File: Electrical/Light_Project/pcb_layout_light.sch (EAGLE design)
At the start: 6 parts, among them U1 REG710NA-3.3/3K, U2 ATTINY85V-10SU

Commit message: Route PCB (not optimized)
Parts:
- added U3: FSM8JRT, button:FSM8JRT
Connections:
- net N$1: now also U3.2
- net N$4: now also U1.ENABLE
- net N$5: now also U3.1
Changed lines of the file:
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@@
 <part name="R1" library="10k Resistor" deviceset="CF14JT10K0" device=""/>
 <part name="C3" library="22ufcap" deviceset="C410C224M5U5TA7200" device=""/>
+<part name="U3" library="button" deviceset="FSM8JRT" device=""/>
 </parts>
 <sheets>
@@
 <attribute name="NAME" x="102.5906" y="88.4428" size="3.4798" layer="95" ratio="10" rot="SR0"/>
 </instance>
+<instance part="U3" gate="A" x="243.84" y="-2.54" smashed="yes" rot="R90">
+<attribute name="NAME" x="234.7214" y="15.5956" size="2.0828" layer="95" ratio="6" rot="SR90"/>
+<attribute name="VALUE" x="237.2614" y="14.9606" size="2.0828" layer="96" ratio="6" rot="SR90"/>
+</instance>
 </instances>
 <busses>
@@
 <pinref part="U2" gate="A" pin="VCC"/>
 <wire x1="7.62" y1="27.94" x2="218.44" y2="27.94" width="0.1524" layer="91"/>
-<wire x1="218.44" y1="27.94" x2="218.44" y2="10.16" width="0.1524" layer="91"/>
+<wire x1="218.44" y1="27.94" x2="218.44" y2="-5.08" width="0.1524" layer="91"/>
 <junction x="7.62" y="91.44"/>
 <junction x="218.44" y="-5.08"/>
-<junction x="218.44" y="10.16"/>
-<wire x1="218.44" y1="10.16" x2="218.44" y2="-5.08" width="0.1524" layer="91"/>
-<wire x1="218.44" y1="10.16" x2="228.6" y2="10.16" width="0.1524" layer="91"/>
-<wire x1="228.6" y1="10.16" x2="228.6" y2="-2.54" width="0.1524" layer="91"/>
-<junction x="228.6" y="-2.54"/>
+<wire x1="218.44" y1="27.94" x2="218.44" y2="43.18" width="0.1524" layer="91"/>
+<junction x="218.44" y="27.94"/>
+<wire x1="218.44" y1="43.18" x2="243.84" y2="43.18" width="0.1524" layer="91"/>
+<pinref part="U3" gate="A" pin="2"/>
+<wire x1="243.84" y1="43.18" x2="243.84" y2="40.64" width="0.1524" layer="91"/>
 </segment>
 </net>
@@
 <junction x="78.74" y="83.82"/>
 <junction x="86.36" y="96.52"/>
+<pinref part="U1" gate="A" pin="ENABLE"/>
+<wire x1="12.7" y1="81.28" x2="12.7" y2="71.12" width="0.1524" layer="91"/>
+<wire x1="12.7" y1="71.12" x2="86.36" y2="71.12" width="0.1524" layer="91"/>
+<wire x1="86.36" y1="71.12" x2="86.36" y2="83.82" width="0.1524" layer="91"/>
+<junction x="86.36" y="83.82"/>
 </segment>
 </net>
@@
 <junction x="218.44" y="-12.7"/>
 <junction x="228.6" y="-12.7"/>
+<pinref part="U3" gate="A" pin="1"/>
+<wire x1="228.6" y1="-12.7" x2="243.84" y2="-12.7" width="0.1524" layer="91"/>
+<wire x1="243.84" y1="-12.7" x2="243.84" y2="0" width="0.1524" layer="91"/>
 </segment>
 </net>

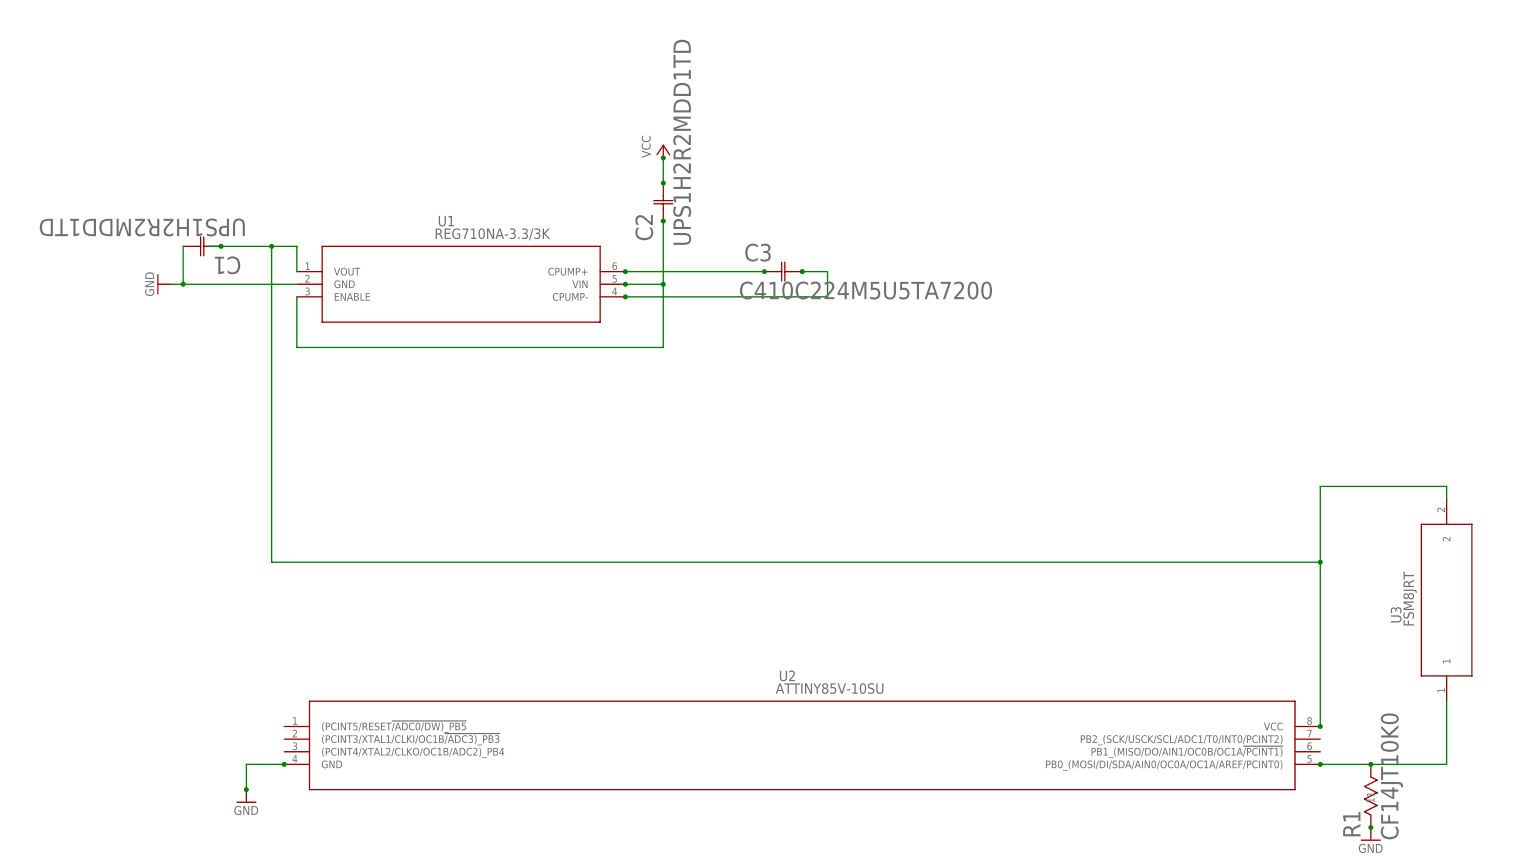
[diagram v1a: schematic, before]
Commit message: use surface mount resistor in diagram
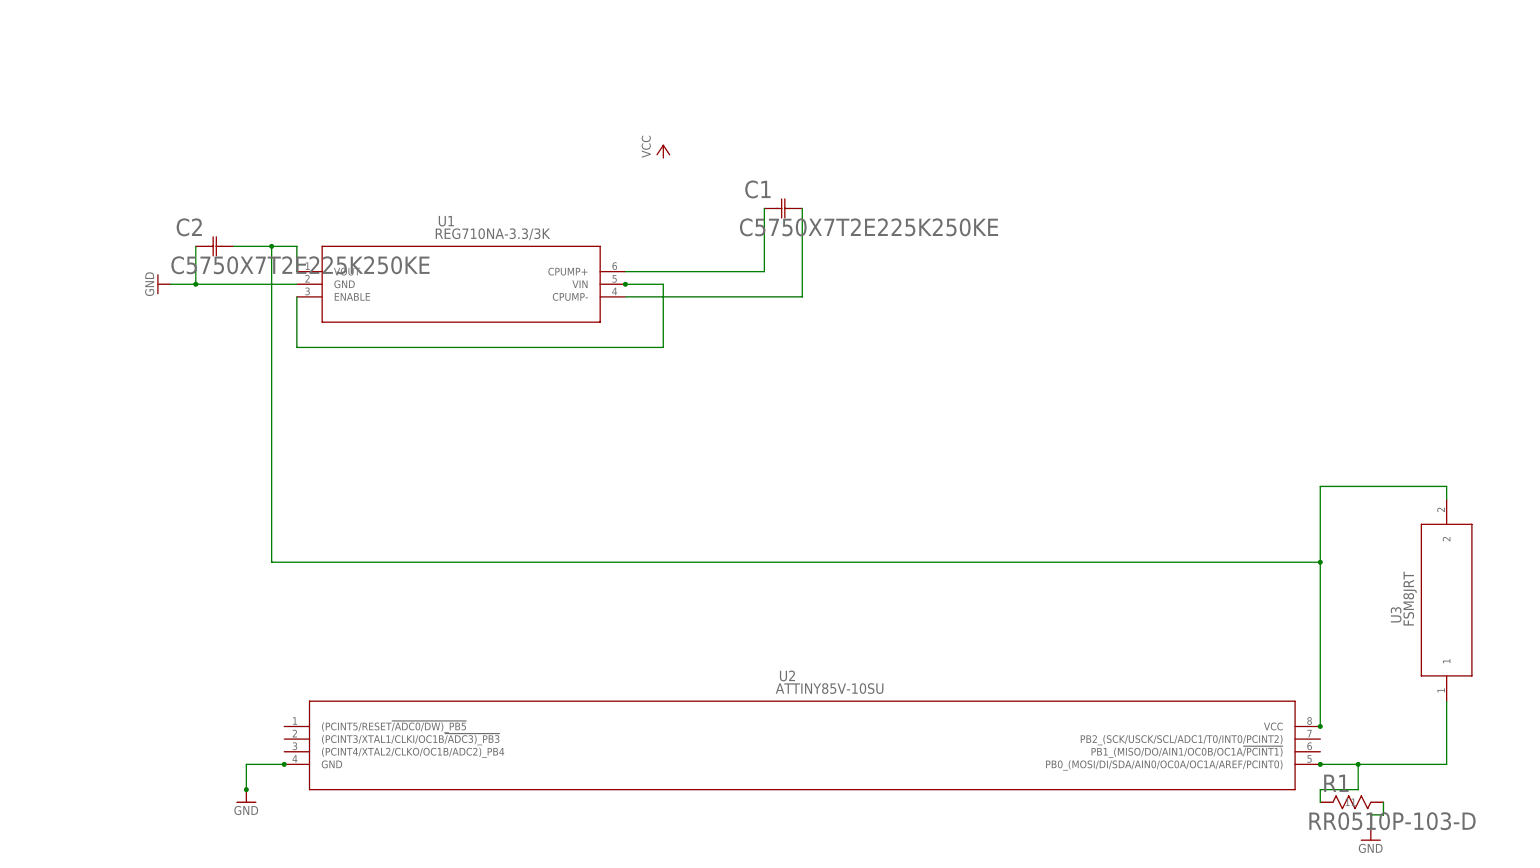
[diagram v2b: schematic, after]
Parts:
- removed C3: C410C224M5U5TA7200, 22ufcap:C410C224M5U5TA7200
- C1, C2: value UPS1H2R2MDD1TD -> C5750X7T2E225K250KE; device 2.2ufCap:UPS1H2R2MDD1TD -> 2p2SFcap:C5750X7T2E225K250KE
- R1: value CF14JT10K0 -> RR0510P-103-D; device 10k Resistor:CF14JT10K0 -> 10kresistor:RR0510P-103-D
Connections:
- removed net VCC: C2.22
- net GND: now also C2.11, R1.22; no longer C1.22, R1.11
- net N$1: now also C2.22; no longer C1.11
- net N$2: now also C1.11; no longer C3.11
- net N$3: now also C1.22; no longer C3.22
- net N$4: no longer C2.11
- net N$5: now also R1.11; no longer R1.22
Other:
- moved on the sheet: C1, C2, R1
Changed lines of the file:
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@@
 <part name="U2" library="attiny85" deviceset="ATTINY85V-10SU" device=""/>
 <part name="GND1" library="supply1" library_urn="urn:adsk.eagle:library:371" deviceset="GND" device=""/>
-<part name="C1" library="2.2ufCap" deviceset="UPS1H2R2MDD1TD" device=""/>
-<part name="C2" library="2.2ufCap" deviceset="UPS1H2R2MDD1TD" device=""/>
 <part name="P+1" library="supply1" library_urn="urn:adsk.eagle:library:371" deviceset="VCC" device=""/>
 <part name="GND2" library="supply1" library_urn="urn:adsk.eagle:library:371" deviceset="GND" device=""/>
 <part name="GND3" library="supply1" library_urn="urn:adsk.eagle:library:371" deviceset="GND" device=""/>
-<part name="R1" library="10k Resistor" deviceset="CF14JT10K0" device=""/>
-<part name="C3" library="22ufcap" deviceset="C410C224M5U5TA7200" device=""/>
 <part name="U3" library="button" deviceset="FSM8JRT" device=""/>
+<part name="R1" library="10kresistor" deviceset="RR0510P-103-D" device=""/>
+<part name="C1" library="2p2SFcap" deviceset="C5750X7T2E225K250KE" device=""/>
+<part name="C2" library="2p2SFcap" deviceset="C5750X7T2E225K250KE" device=""/>
 </parts>
 <sheets>
@@
 <attribute name="VALUE" x="-17.78" y="86.36" size="1.778" layer="96" rot="R270"/>
 </instance>
-<instance part="C1" gate="A" x="-2.54" y="91.44" smashed="yes" rot="R180">
-<attribute name="VALUE" x="2.6162" y="96.9772" size="3.4798" layer="96" ratio="10" rot="SR180"/>
-<attribute name="NAME" x="1.5494" y="89.3572" size="3.4798" layer="95" ratio="10" rot="SR180"/>
-</instance>
-<instance part="C2" gate="A" x="86.36" y="96.52" smashed="yes" rot="R90">
-<attribute name="VALUE" x="91.8972" y="91.3638" size="3.4798" layer="96" ratio="10" rot="SR90"/>
-<attribute name="NAME" x="84.2772" y="92.4306" size="3.4798" layer="95" ratio="10" rot="SR90"/>
-</instance>
 <instance part="P+1" gate="VCC" x="86.36" y="111.76" smashed="yes">
 <attribute name="VALUE" x="83.82" y="109.22" size="1.778" layer="96" rot="R90"/>
@@
 <attribute name="VALUE" x="226.06" y="-30.48" size="1.778" layer="96"/>
 </instance>
-<instance part="R1" gate="A" x="228.6" y="-25.4" smashed="yes" rot="R90">
-<attribute name="VALUE" x="234.1372" y="-28.0162" size="3.4798" layer="96" ratio="10" rot="SR90"/>
-<attribute name="NAME" x="226.5172" y="-27.5844" size="3.4798" layer="95" ratio="10" rot="SR90"/>
-</instance>
-<instance part="C3" gate="A" x="106.68" y="86.36" smashed="yes">
-<attribute name="VALUE" x="101.5238" y="80.8228" size="3.4798" layer="96" ratio="10" rot="SR0"/>
-<attribute name="NAME" x="102.5906" y="88.4428" size="3.4798" layer="95" ratio="10" rot="SR0"/>
-</instance>
 <instance part="U3" gate="A" x="243.84" y="-2.54" smashed="yes" rot="R90">
 <attribute name="NAME" x="234.7214" y="15.5956" size="2.0828" layer="95" ratio="6" rot="SR90"/>
 <attribute name="VALUE" x="237.2614" y="14.9606" size="2.0828" layer="96" ratio="6" rot="SR90"/>
+</instance>
+<instance part="R1" gate="A" x="218.44" y="-20.32" smashed="yes">
+<attribute name="VALUE" x="215.8238" y="-25.8572" size="3.4798" layer="96" ratio="10" rot="SR0"/>
+<attribute name="NAME" x="218.7956" y="-18.2372" size="3.4798" layer="95" ratio="10" rot="SR0"/>
+</instance>
+<instance part="C1" gate="A" x="106.68" y="99.06" smashed="yes">
+<attribute name="VALUE" x="101.5238" y="93.5228" size="3.4798" layer="96" ratio="10" rot="SR0"/>
+<attribute name="NAME" x="102.5906" y="101.1428" size="3.4798" layer="95" ratio="10" rot="SR0"/>
+</instance>
+<instance part="C2" gate="A" x="-7.62" y="91.44" smashed="yes">
+<attribute name="VALUE" x="-12.7762" y="85.9028" size="3.4798" layer="96" ratio="10" rot="SR0"/>
+<attribute name="NAME" x="-11.7094" y="93.5228" size="3.4798" layer="95" ratio="10" rot="SR0"/>
 </instance>
 </instances>
@@
 <pinref part="GND1" gate="1" pin="GND"/>
 <pinref part="U1" gate="A" pin="GND"/>
-<wire x1="-12.7" y1="83.82" x2="-10.16" y2="83.82" width="0.1524" layer="91"/>
-<pinref part="C1" gate="A" pin="22"/>
-<wire x1="-10.16" y1="83.82" x2="12.7" y2="83.82" width="0.1524" layer="91"/>
-<wire x1="-10.16" y1="91.44" x2="-10.16" y2="83.82" width="0.1524" layer="91"/>
-<junction x="-10.16" y="83.82"/>
+<wire x1="-12.7" y1="83.82" x2="-7.62" y2="83.82" width="0.1524" layer="91"/>
+<pinref part="C2" gate="A" pin="11"/>
+<wire x1="-7.62" y1="83.82" x2="12.7" y2="83.82" width="0.1524" layer="91"/>
+<wire x1="-7.62" y1="91.44" x2="-7.62" y2="83.82" width="0.1524" layer="91"/>
+<junction x="-7.62" y="83.82"/>
 </segment>
 <segment>
@@
 <segment>
 <pinref part="GND3" gate="1" pin="GND"/>
-<pinref part="R1" gate="A" pin="11"/>
-<junction x="228.6" y="-25.4"/>
+<wire x1="228.6" y1="-22.86" x2="228.6" y2="-25.4" width="0.1524" layer="91"/>
+<pinref part="R1" gate="A" pin="22"/>
+<wire x1="231.14" y1="-20.32" x2="231.14" y2="-22.86" width="0.1524" layer="91"/>
+<wire x1="231.14" y1="-22.86" x2="228.6" y2="-22.86" width="0.1524" layer="91"/>
 </segment>
 </net>
@@
 <wire x1="12.7" y1="86.36" x2="12.7" y2="91.44" width="0.1524" layer="91"/>
 <wire x1="12.7" y1="91.44" x2="7.62" y2="91.44" width="0.1524" layer="91"/>
-<pinref part="C1" gate="A" pin="11"/>
-<wire x1="-2.54" y1="91.44" x2="-5.08" y2="91.44" width="0.1524" layer="91"/>
-<junction x="-2.54" y="91.44"/>
-<wire x1="-2.54" y1="91.44" x2="7.62" y2="91.44" width="0.1524" layer="91"/>
 <wire x1="7.62" y1="91.44" x2="7.62" y2="27.94" width="0.1524" layer="91"/>
 <pinref part="U2" gate="A" pin="VCC"/>
 <wire x1="7.62" y1="27.94" x2="218.44" y2="27.94" width="0.1524" layer="91"/>
 <wire x1="218.44" y1="27.94" x2="218.44" y2="-5.08" width="0.1524" layer="91"/>
-<junction x="7.62" y="91.44"/>
 <junction x="218.44" y="-5.08"/>
 <wire x1="218.44" y1="27.94" x2="218.44" y2="43.18" width="0.1524" layer="91"/>
@@
 <pinref part="U3" gate="A" pin="2"/>
 <wire x1="243.84" y1="43.18" x2="243.84" y2="40.64" width="0.1524" layer="91"/>
+<pinref part="C2" gate="A" pin="22"/>
+<wire x1="0" y1="91.44" x2="7.62" y2="91.44" width="0.1524" layer="91"/>
+<junction x="7.62" y="91.44"/>
+</segment>
+</net>
+<net name="N$4" class="0">
+<segment>
+<pinref part="U1" gate="A" pin="VIN"/>
+<wire x1="78.74" y1="83.82" x2="86.36" y2="83.82" width="0.1524" layer="91"/>
+<junction x="78.74" y="83.82"/>
+<pinref part="U1" gate="A" pin="ENABLE"/>
+<wire x1="12.7" y1="81.28" x2="12.7" y2="71.12" width="0.1524" layer="91"/>
+<wire x1="12.7" y1="71.12" x2="86.36" y2="71.12" width="0.1524" layer="91"/>
+<wire x1="86.36" y1="71.12" x2="86.36" y2="83.82" width="0.1524" layer="91"/>
+</segment>
+</net>
+<net name="N$5" class="0">
+<segment>
+<pinref part="U2" gate="A" pin="PB0_(MOSI/DI/SDA/AIN0/OC0A/OC1A/AREF/PCINT0)"/>
+<junction x="218.44" y="-12.7"/>
+<pinref part="U3" gate="A" pin="1"/>
+<wire x1="218.44" y1="-12.7" x2="226.06" y2="-12.7" width="0.1524" layer="91"/>
+<wire x1="226.06" y1="-12.7" x2="243.84" y2="-12.7" width="0.1524" layer="91"/>
+<wire x1="243.84" y1="-12.7" x2="243.84" y2="0" width="0.1524" layer="91"/>
+<pinref part="R1" gate="A" pin="11"/>
+<wire x1="218.44" y1="-20.32" x2="218.44" y2="-17.78" width="0.1524" layer="91"/>
+<wire x1="218.44" y1="-17.78" x2="226.06" y2="-17.78" width="0.1524" layer="91"/>
+<wire x1="226.06" y1="-17.78" x2="226.06" y2="-12.7" width="0.1524" layer="91"/>
+<junction x="226.06" y="-12.7"/>
 </segment>
 </net>
@@
 <pinref part="U1" gate="A" pin="CPUMP+"/>
 <wire x1="78.74" y1="86.36" x2="106.68" y2="86.36" width="0.1524" layer="91"/>
-<junction x="78.74" y="86.36"/>
-<pinref part="C3" gate="A" pin="11"/>
-<junction x="106.68" y="86.36"/>
+<pinref part="C1" gate="A" pin="11"/>
+<wire x1="106.68" y1="86.36" x2="106.68" y2="99.06" width="0.1524" layer="91"/>
 </segment>
 </net>
@@
 <segment>
 <pinref part="U1" gate="A" pin="CPUMP-"/>
-<wire x1="78.74" y1="81.28" x2="119.38" y2="81.28" width="0.1524" layer="91"/>
-<wire x1="119.38" y1="81.28" x2="119.38" y2="86.36" width="0.1524" layer="91"/>
-<wire x1="119.38" y1="86.36" x2="114.3" y2="86.36" width="0.1524" layer="91"/>
-<junction x="78.74" y="81.28"/>
-<pinref part="C3" gate="A" pin="22"/>
-<junction x="114.3" y="86.36"/>
+<wire x1="114.3" y1="81.28" x2="78.74" y2="81.28" width="0.1524" layer="91"/>
+<pinref part="C1" gate="A" pin="22"/>
+<wire x1="114.3" y1="99.06" x2="114.3" y2="81.28" width="0.1524" layer="91"/>
 </segment>
 </net>
-<net name="N$4" class="0">
-<segment>
-<pinref part="U1" gate="A" pin="VIN"/>
-<wire x1="78.74" y1="83.82" x2="86.36" y2="83.82" width="0.1524" layer="91"/>
-<pinref part="C2" gate="A" pin="11"/>
-<wire x1="86.36" y1="83.82" x2="86.36" y2="96.52" width="0.1524" layer="91"/>
-<junction x="78.74" y="83.82"/>
-<junction x="86.36" y="96.52"/>
-<pinref part="U1" gate="A" pin="ENABLE"/>
-<wire x1="12.7" y1="81.28" x2="12.7" y2="71.12" width="0.1524" layer="91"/>
-<wire x1="12.7" y1="71.12" x2="86.36" y2="71.12" width="0.1524" layer="91"/>
-<wire x1="86.36" y1="71.12" x2="86.36" y2="83.82" width="0.1524" layer="91"/>
-<junction x="86.36" y="83.82"/>
-</segment>
-</net>
-<net name="VCC" class="0">
-<segment>
-<pinref part="P+1" gate="VCC" pin="VCC"/>
-<pinref part="C2" gate="A" pin="22"/>
-<wire x1="86.36" y1="109.22" x2="86.36" y2="104.14" width="0.1524" layer="91"/>
-<junction x="86.36" y="104.14"/>
-<junction x="86.36" y="109.22"/>
-</segment>
-</net>
-<net name="N$5" class="0">
-<segment>
-<pinref part="U2" gate="A" pin="PB0_(MOSI/DI/SDA/AIN0/OC0A/OC1A/AREF/PCINT0)"/>
-<pinref part="R1" gate="A" pin="22"/>
-<wire x1="218.44" y1="-12.7" x2="228.6" y2="-12.7" width="0.1524" layer="91"/>
-<junction x="218.44" y="-12.7"/>
-<junction x="228.6" y="-12.7"/>
-<pinref part="U3" gate="A" pin="1"/>
-<wire x1="228.6" y1="-12.7" x2="243.84" y2="-12.7" width="0.1524" layer="91"/>
-<wire x1="243.84" y1="-12.7" x2="243.84" y2="0" width="0.1524" layer="91"/>
-</segment>
-</net>
